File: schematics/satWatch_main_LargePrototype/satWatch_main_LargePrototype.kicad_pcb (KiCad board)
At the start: 2 copper layers, 138.8 x 55.2 mm, 121 parts, among them J1 PogoPins_02x17_Data, J2 UJ20-C-H-G-MSMT-2B-P16-TR, J5 Pogo_02x03_Power, Q1 FS8205, Q2 BSS138, Q3 DMP1045U, Q4 BSS138, SW1 B3U-1000P, SW2 B3U-1000P, SW3 B3U-1000P, SW4 B3U-1000P, SW5 B3U-1000P, U1 ESP32-S3-MINI-1, U10 VEMD8080, U11 VEMD8080, U12 BNO085, U2 MAX86141, U3 MAX32664GTGC, U4 NCP186AMX330TAG, U5 DS3231MZ, U6 MIC5365-1.8YC5, U7 PAM2401SCADJ, U8 TP4056-42-ESOP8, U9 DW01A, Y1 32.768kHz, Y2 32.768Hz

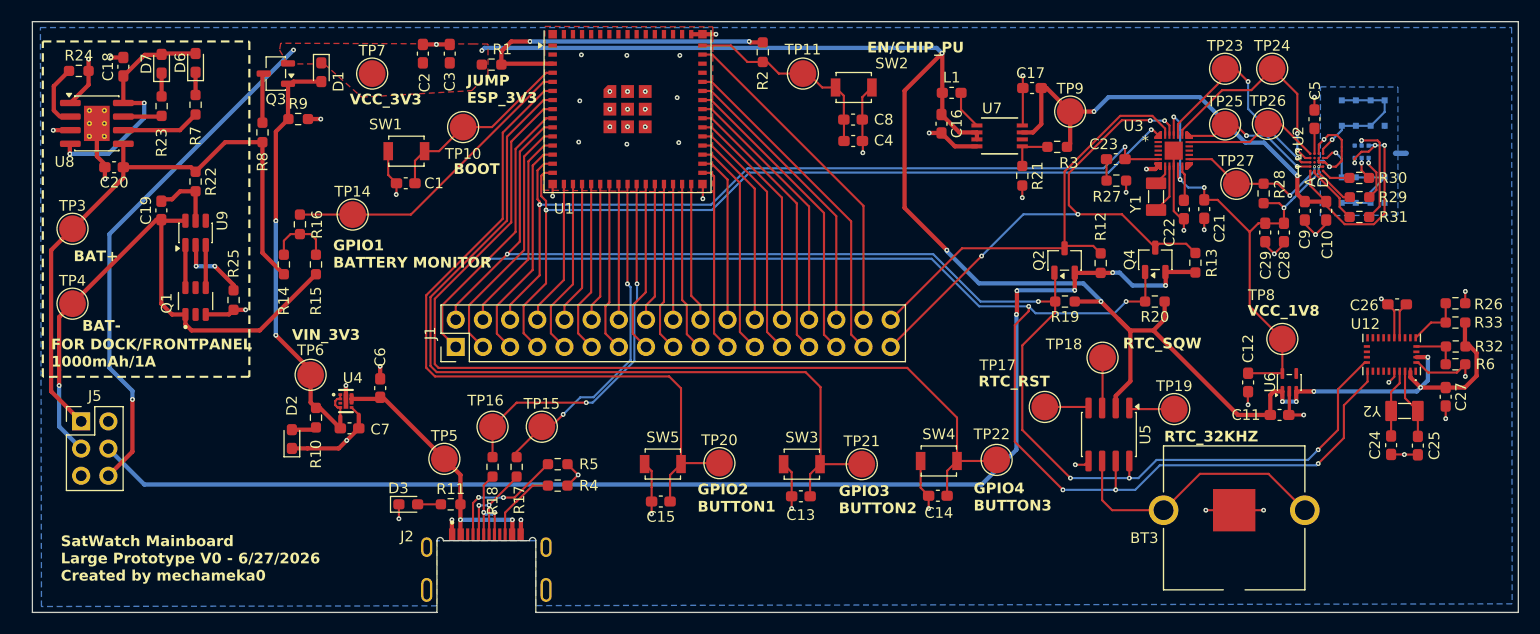
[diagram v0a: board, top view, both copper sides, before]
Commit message: v0.5
removed MAX3264/MAX86141 for MAX30101 for reduced scope. editted PCB and via sizes based on manufacturer response.
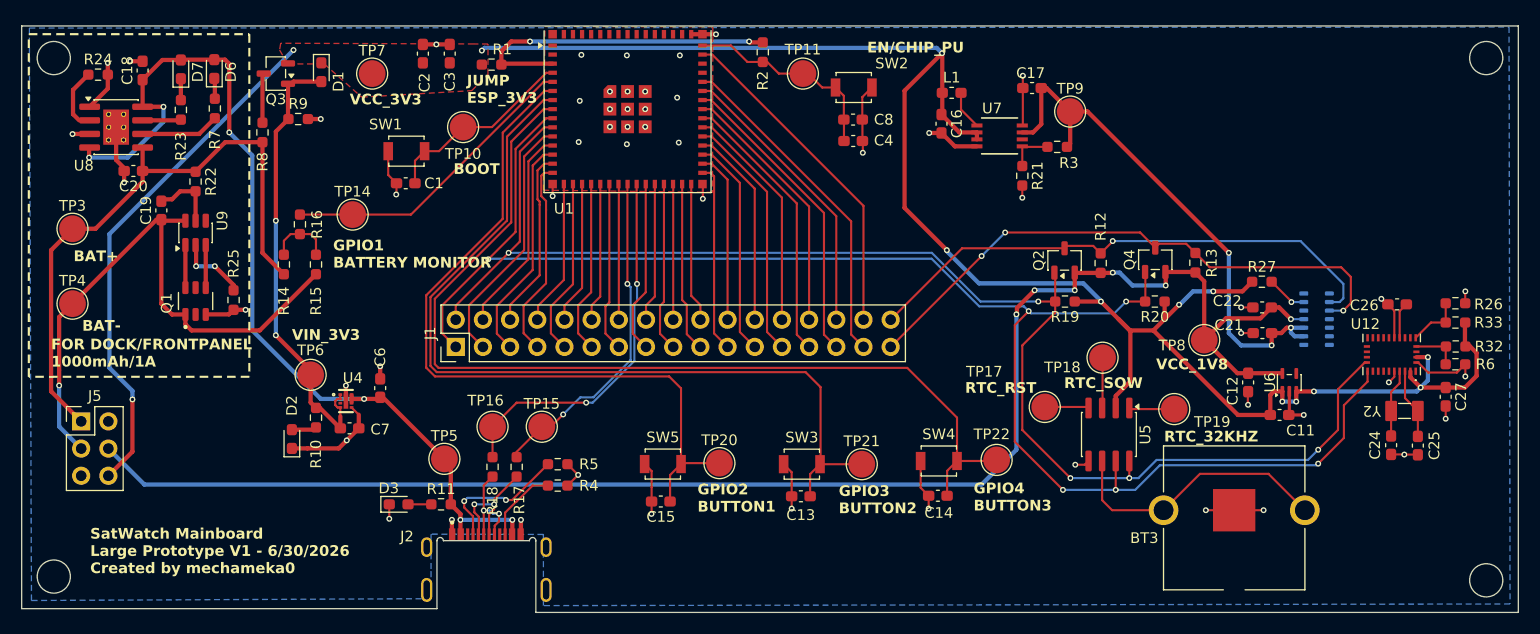
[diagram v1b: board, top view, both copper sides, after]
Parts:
- removed C10, C29: 0.1uF, Capacitor_SMD:C_0603_1608Metric_Pad1.08x0.95mm_HandSolder
- removed C23: 1uF, Capacitor_SMD:C_0603_1608Metric_Pad1.08x0.95mm_HandSolder
- removed C28: 22uF, Capacitor_SMD:C_0603_1608Metric_Pad1.08x0.95mm_HandSolder
- removed C5, C9: 10uF, Capacitor_SMD:C_0603_1608Metric_Pad1.08x0.95mm_HandSolder
- removed LED1: SFH 7016, footprint:SFH7016
- removed NT1: NetTie_2, footprint:NetTie-2_SMD_Pad0.2mm
- removed NT1: NetTie_2, NetTie:NetTie-2_SMD_Pad0.5mm
- removed R28: 100K, Resistor_SMD:R_0603_1608Metric_Pad0.98x0.95mm_HandSolder
- removed R29, R30, R31: 0, Resistor_SMD:R_0603_1608Metric_Pad0.98x0.95mm_HandSolder
- removed TP23: PPG_MISO, TestPoint:TestPoint_Pad_D2.5mm
- removed TP24: PPG_MOSI, TestPoint:TestPoint_Pad_D2.5mm
- removed TP25: PPG_SCK, TestPoint:TestPoint_Pad_D2.5mm
- removed TP26: PPG_CSB, TestPoint:TestPoint_Pad_D2.5mm
- removed TP27: PPG_INT, TestPoint:TestPoint_Pad_D2.5mm
- removed U10, U11: VEMD8080, footprint:VEMD8080
- removed U3: MAX32664GTGC, footprint:MAX32664GTGB+T
- removed Y1: 32.768kHz, footprint:ABS07-32.768KHZ-T
- C21: value 1uF -> 10uF
- C22: value 1uF -> 0.1uF
- R27: value 10 -> 4.7K
- U2: value MAX86141 -> MAX30101EFD_T; footprint footprint:MAX86141ENP -> footprint:MAX30101EFD+T; moved to B.Cu
- moved R27 16.6 mm to (194.9, 88.5), turned to 180 degrees
- moved U2 14.7 mm to (200.0, 92.0), turned to 180 degrees
- moved C21 12.8 mm to (194.9, 93.2), turned to 180 degrees
- moved C22 11.7 mm to (194.9, 90.8), turned to 180 degrees
- moved TP8 7.30 mm to (189.5, 93.9)
- moved D7 1.87 mm to (93.9, 68.6)
- moved D6 1.84 mm to (97.0, 68.6)
- moved C18 1.83 mm to (90.3, 68.7)
- moved R7 1.83 mm to (97.0, 72.3)
- moved C20 1.83 mm to (89.4, 78.1)
- moved R23 1.83 mm to (93.9, 72.4)
- moved R24 1.83 mm to (86.1, 69.1)
- moved U8 1.83 mm to (87.8, 74.0)
- moved D3 0.90 mm to (114.2, 109.2)
- moved R11 0.90 mm to (118.2, 109.2)
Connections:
- net /ESP_3V3 renamed ESP_3V3
- net /VIN_3V3 renamed VIN_3V3
- C18 pad 1: /VUSB_5V -> USB_5V
- C21 pad 1: 1V8 -> 5V
- C22 pad 1: Net-(U3-VCORE) -> 1V8
- D6 pad 2: /VUSB_5V -> USB_5V
- D7 pad 2: /VUSB_5V -> USB_5V
- J5 pad 4: /VCC_1V8 -> 1V8
- Q2 pad 2: /VCC_1V8 -> 1V8
- Q4 pad 2: /VCC_1V8 -> 1V8
- R12 pad 1: /VCC_1V8 -> 1V8
- R13 pad 1: /VCC_1V8 -> 1V8
- R27 pad 1: Net-(C23-Pad2) -> Net-(U2-~{INT})
- R27 pad 2: GND -> VCC_3V3
- U8 pad 4: /VUSB_5V -> USB_5V
- U8 pad 8: /VUSB_5V -> USB_5V
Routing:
- net /VCC_1V8: track 122.4 -> 0.00 mm, vias 5 -> 0
- net 1V8: track 48.7 -> 147.8 mm, vias 5 -> 6
- net USB_5V: track 25.7 -> 88.7 mm, vias 2 -> 6
- net /GPIO10: track 78.0 -> 16.8 mm, vias 2 -> 0
- net /GPIO11: track 79.4 -> 18.8 mm, vias 2 -> 0
- net /VUSB_5V: track 22.8 -> 0.00 mm, vias 2 -> 0
- net GND: track 132.7 -> 110.7 mm, vias 61 -> 55
- net /PPG_MOSI: track 21.4 -> 0.00 mm, vias 2 -> 0
- net /PPG_MISO: track 21.2 -> 0.00 mm, vias 2 -> 0
- net /PPG_INT: track 14.5 -> 0.00 mm, vias 2 -> 0
- net /PD2_IN: track 13.6 -> 0.00 mm, vias 1 -> 0
- net /PPG_SCK: track 13.5 -> 0.00 mm, vias 2 -> 0
- net /PPG_CSB: track 13.2 -> 0.00 mm
- net /PD1_IN: track 13.0 -> 0.00 mm, vias 1 -> 0
- net 5V: track 63.7 -> 50.9 mm, vias 5 -> 3
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- removed copper zone on B.Cu, net /PD_GND
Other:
- board size 138.8 x 55.2 mm -> 139.8 x 54.8 mm
- board text added: "SatWatch Mainboard Large Prototype V1 - 6/30/2026 Created by mechameka0"
- board text removed: "SatWatch Mainboard Large Prototype V0 - 6/27/2026 Created by mechameka0"
